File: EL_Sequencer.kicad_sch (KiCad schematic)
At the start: 177 parts, among them J1 B2B-PH-K-S, J10 Header_01x02_Male, J11 Header_01x02_Male, J12 Header_01x02_Male, J13 Header_01x02_Male, J14 Header_01x02_Male, J15 Header_01x02_Male, J16 Header_01x02_Male, J17 Header_01x02_Male, J18 Header_01x02_Male, J19 Header_01x02_Male, J2 Conn_01x06, J20 Header_01x02_Male, J21 Header_01x02_Male, J22 Header_01x02_Male, J23 Header_01x02_Male, J24 Header_01x02_Male, J25 Header_01x02_Male, J26 Header_01x02_Male, J27 Header_01x02_Male, J28 Header_01x02_Male, J29 Header_01x02_Male, J3 Header_01x02_Male, J4 Header_01x02_Male, J5 Conn2x5_CNC#3220-10-0100-00, J6 Header_01x02_Male, J7 Header_01x02_Male, J8 Header_01x02_Male, J9 Header_01x02_Male, Q1 Z0103NN, Q10 Z0103NN, Q11 Z0103NN, Q12 Z0103NN, Q13 Z0103NN, Q14 Z0103NN, Q15 Z0103NN, Q16 Z0103NN, Q17 Z0103NN, Q18 Z0103NN, Q19 Z0103NN, Q2 Z0103NN, Q20 Z0103NN, Q21 Z0103NN, Q22 Z0103NN, Q23 Z0103NN, Q24 Z0103NN, Q3 Z0103NN, Q4 Z0103NN, Q5 Z0103NN, Q6 Z0103NN, Q7 Z0103NN, Q8 Z0103NN, Q9 Z0103NN, SW1 FSM2JSMAA, U1 ATmega1284-AU, U10 MOC3063SM, U11 MOC3063SM, U12 MOC3063SM, U13 MOC3063SM, U14 MOC3063SM, U15 MOC3063SM, U16 MOC3063SM, U17 MOC3063SM, U18 MOC3063SM, U19 MOC3063SM, U2 NCP718BSN330T1G, U20 MOC3063SM, U21 MOC3063SM, U22 MOC3063SM, U23 MOC3063SM, U24 MOC3063SM, U25 MOC3063SM, U26 MOC3063SM, U3 MOC3063SM, U4 MOC3063SM, U5 MOC3063SM, U6 MOC3063SM, U7 MOC3063SM, U8 MOC3063SM, U9 MOC3063SM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

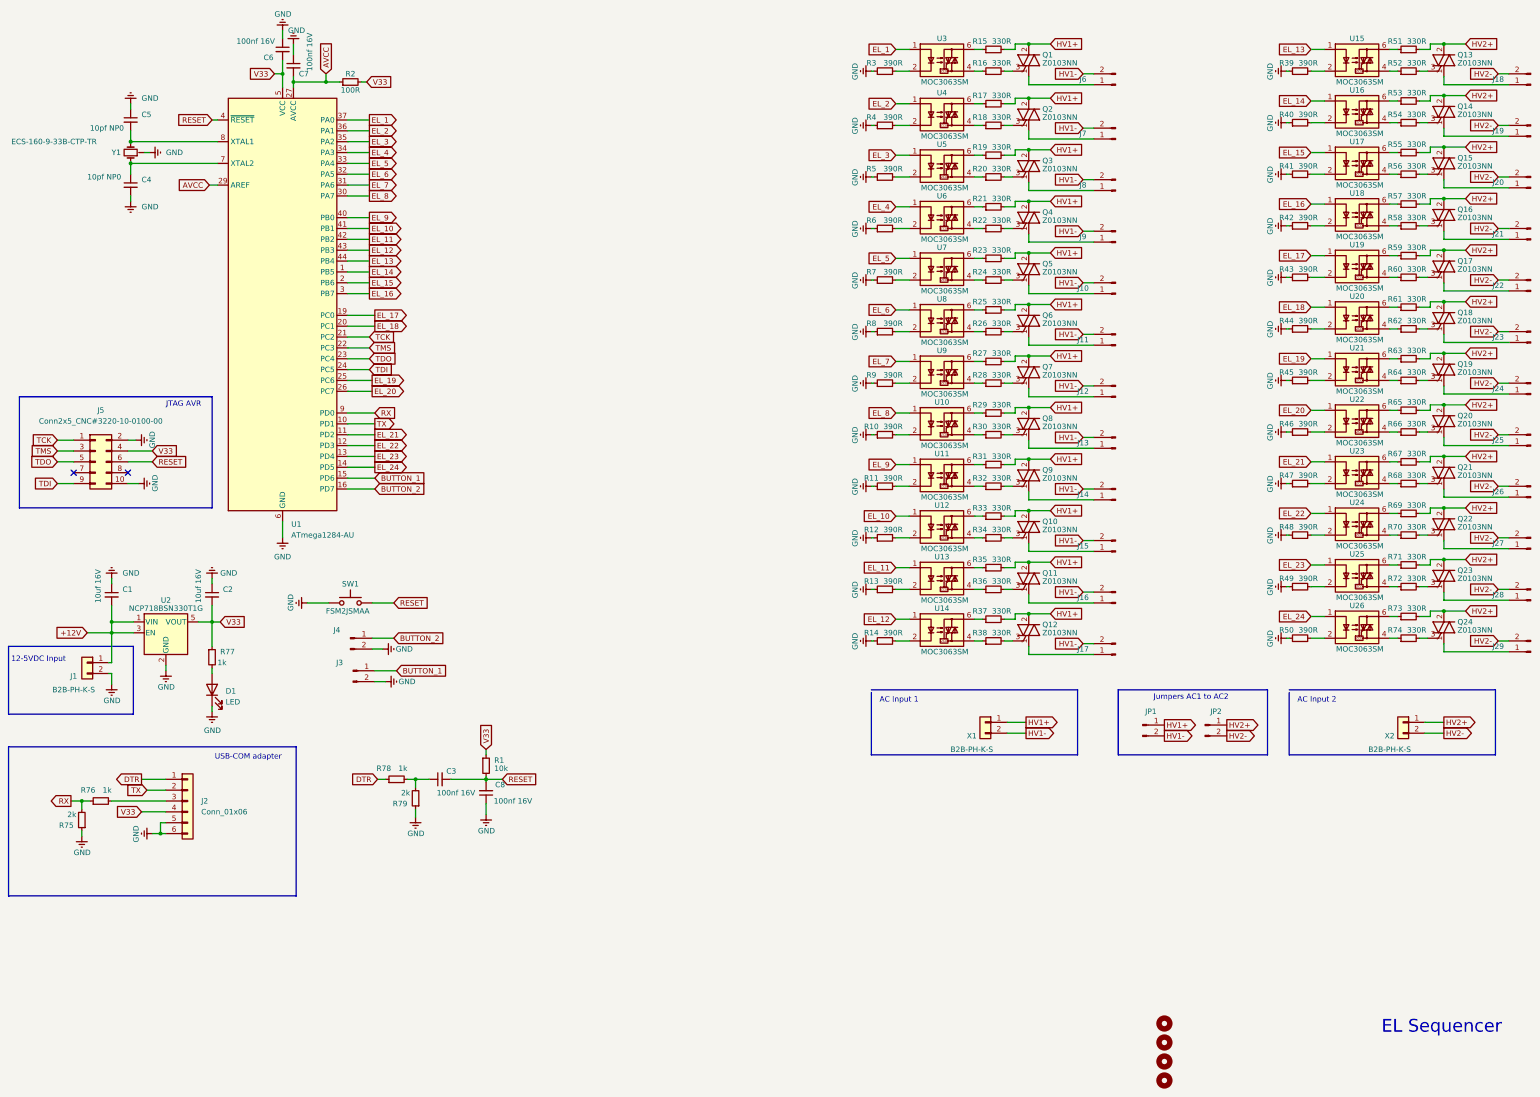
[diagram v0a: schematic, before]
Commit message: Arduino compatible and smaller
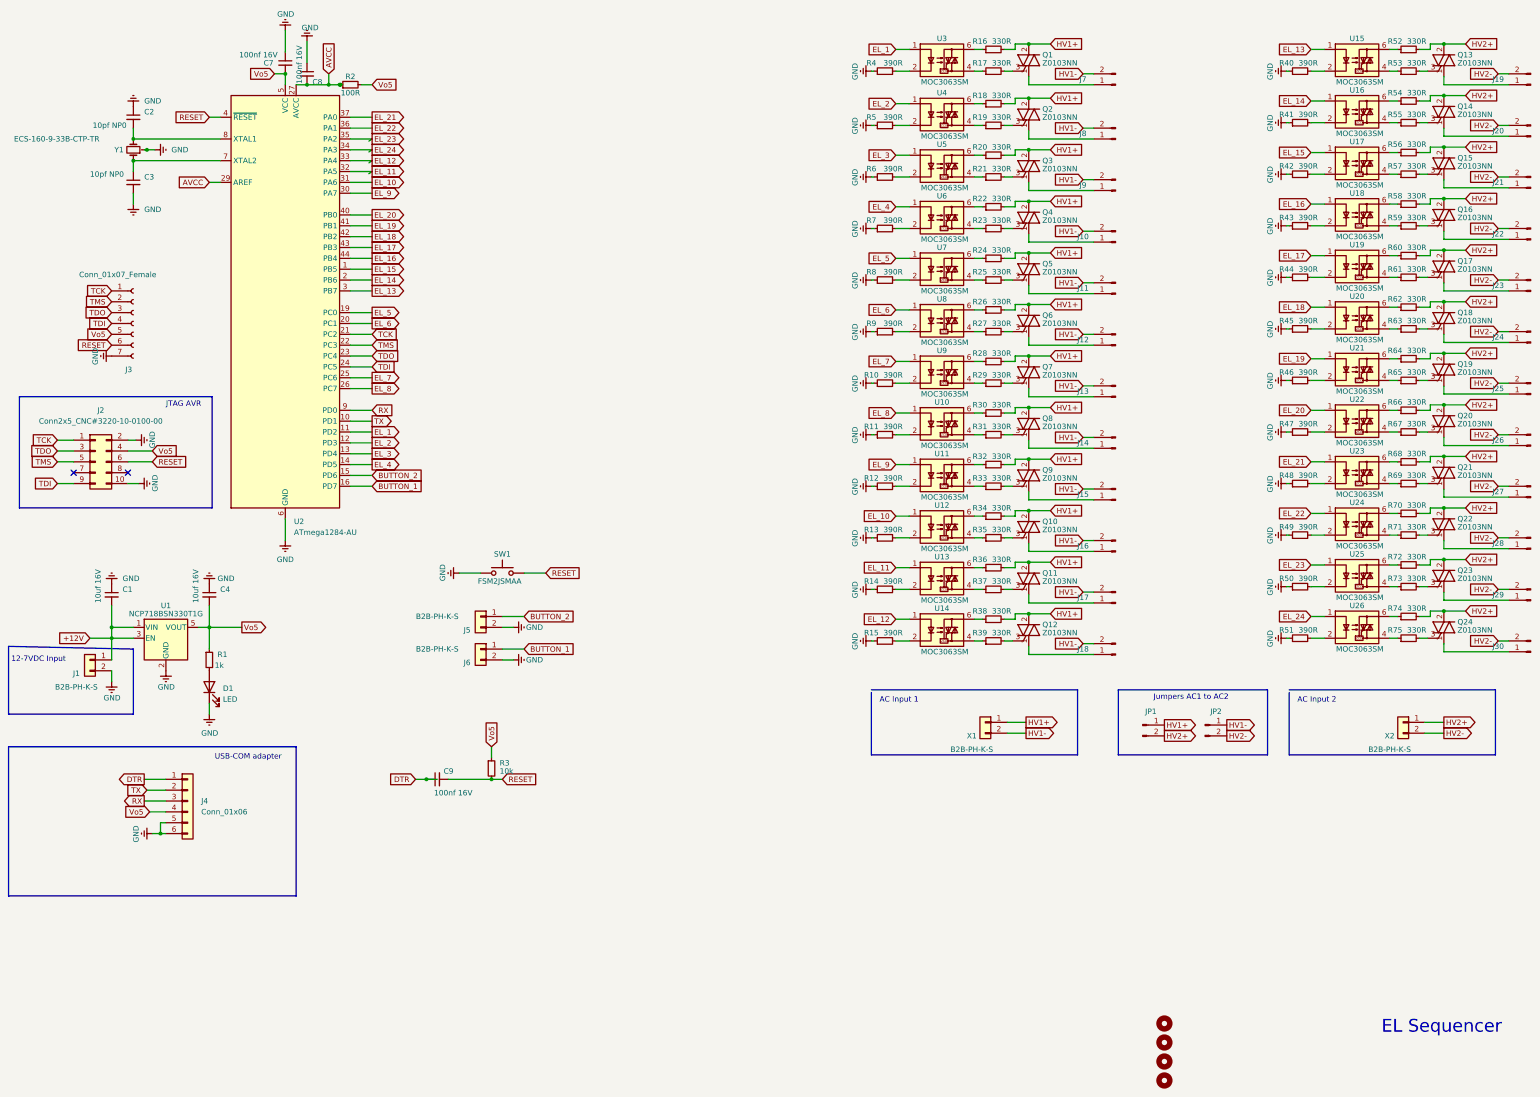
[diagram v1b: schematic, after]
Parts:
- removed C8: 100nf 16V, Capacitor_SMD:C_0805_2012Metric, symbol Device:C_Small
- removed J3, J4: Header_01x02_Male, Connector_PinHeader_2.54mm:PinHeader_1x02_P2.54mm_Vertical, symbol Connector:Conn_01x02_Male
- removed R75, R79: 2k, Resistor_SMD:R_0805_2012Metric, symbol Device:R_Small
- removed R76, R78: 1k, Resistor_SMD:R_0805_2012Metric, symbol Device:R_Small
- added J3: Conn_01x07_Female, Connector_PinHeader_2.54mm:PinHeader_1x07_P2.54mm_Vertical, symbol Connector:Conn_01x07_Female
- added J5, J6: B2B-PH-K-S, Connector_JST:JST_PH_B2B-PH-K_1x02_P2.00mm_Vertical, symbol Connector_Generic:Conn_01x02
- Q1: LCSC (none) -> C602954
- U1: renamed from U2; LCSC (none) -> C892795
- U2: renamed from U1; LCSC (none) -> C33575
- U3: LCSC (none) -> C77950
- renumbered C5 to C2, C4 to C3, C2 to C4, C6 to C7, C7 to C8, C3 to C9, J9 to J10, J10 to J11, J11 to J12, J12 to J13, J13 to J14, J14 to J15, J15 to J16, J16 to J17, J17 to J18, J18 to J19, J5 to J2, J19 to J20, J20 to J21, J21 to J22, J22 to J23, J23 to J24, J24 to J25, J25 to J26, J26 to J27, J27 to J28, J28 to J29, J29 to J30, J2 to J4, J6 to J7, J7 to J8, J8 to J9, R77 to R1, R9 to R10, R10 to R11, R11 to R12, R12 to R13, R13 to R14, R14 to R15, R15 to R16, R16 to R17, R17 to R18, R18 to R19, R19 to R20, R20 to R21, R21 to R22, R22 to R23, R23 to R24, R24 to R25, R25 to R26, R26 to R27, R27 to R28, R28 to R29, R1 to R3, R29 to R30, R30 to R31, R31 to R32, R32 to R33, R33 to R34, R34 to R35, R35 to R36, R36 to R37, R37 to R38, R38 to R39, R3 to R4, R39 to R40, R40 to R41, R41 to R42, R42 to R43, R43 to R44, R44 to R45, R45 to R46, R46 to R47, R47 to R48, R48 to R49, R4 to R5, R49 to R50, R50 to R51, R51 to R52, R52 to R53, R53 to R54, R54 to R55, R55 to R56, R56 to R57, R57 to R58, R58 to R59, R5 to R6, R59 to R60, R60 to R61, R61 to R62, R62 to R63, R63 to R64, R64 to R65, R65 to R66, R66 to R67, R67 to R68, R68 to R69, R6 to R7, R69 to R70, R70 to R71, R71 to R72, R72 to R73, R73 to R74, R74 to R75, R7 to R8, R8 to R9
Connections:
- net BUTTON_1: now also U2.16 (PD7), J6.1 (Pin_1); no longer U2.15 (PD6)
- net BUTTON_2: now also U2.15 (PD6), J5.1 (Pin_1); no longer U2.16 (PD7)
- net DTR: now also C9.1
- net EL_1: now also U2.11 (PD2); no longer U2.37 (PA0)
- net EL_10: now also U2.31 (PA6); no longer U2.41 (PB1)
- net EL_11: now also U2.32 (PA5); no longer U2.42 (PB2)
- net EL_12: now also U2.33 (PA4); no longer U2.43 (PB3)
- net EL_13: now also U2.3 (PB7); no longer U2.44 (PB4)
- net EL_14: now also U2.2 (PB6); no longer U2.1 (PB5)
- net EL_15: now also U2.1 (PB5); no longer U2.2 (PB6)
- net EL_16: now also U2.44 (PB4); no longer U2.3 (PB7)
- net EL_17: now also U2.43 (PB3); no longer U2.19 (PC0)
- net EL_18: now also U2.42 (PB2); no longer U2.20 (PC1)
- net EL_19: now also U2.41 (PB1); no longer U2.25 (PC6)
- net EL_2: now also U2.12 (PD3); no longer U2.36 (PA1)
- net EL_20: now also U2.40 (PB0); no longer U2.26 (PC7)
- net EL_21: now also U2.37 (PA0); no longer U2.11 (PD2)
- net EL_22: now also U2.36 (PA1); no longer U2.12 (PD3)
- net EL_23: now also U2.35 (PA2); no longer U2.13 (PD4)
- net EL_24: now also U2.34 (PA3); no longer U2.14 (PD5)
- net EL_3: now also U2.13 (PD4); no longer U2.35 (PA2)
- net EL_4: now also U2.14 (PD5); no longer U2.34 (PA3)
- net EL_5: now also U2.19 (PC0); no longer U2.33 (PA4)
- net EL_6: now also U2.20 (PC1); no longer U2.32 (PA5)
- net EL_7: now also U2.25 (PC6); no longer U2.31 (PA6)
- net EL_8: now also U2.26 (PC7); no longer U2.30 (PA7)
- net EL_9: now also U2.30 (PA7); no longer U2.40 (PB0)
- net GND: now also J3.7 (Pin_7), J5.2 (Pin_2), J6.2 (Pin_2)
- net HV1-: now also JP2.1 (Pin_1); no longer JP1.2 (Pin_2)
- net HV2+: now also JP1.2 (Pin_2); no longer JP2.1 (Pin_1)
- net RESET: now also J3.6 (Pin_6)
- net RX: now also J4.3 (Pin_3)
- net TCK: now also J3.1 (Pin_1)
- net TDI: now also J3.4 (Pin_4)
- net TDO: now also J2.3 (Pin_3), J3.3 (Pin_3); no longer J2.5 (Pin_5)
- net TMS: now also J2.5 (Pin_5), J3.2 (Pin_2); no longer J2.3 (Pin_3)
- net V33 renamed Vo5
- net Vo5: now also J3.5 (Pin_5)
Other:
- note added: "12-7VDC Input"
- note removed: "12-5VDC Input"
- moved on the sheet: C2, C3, C4, C7, C8, C9, D1, J1, R1, R2, R3, SW1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
